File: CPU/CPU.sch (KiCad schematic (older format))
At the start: 12 parts, among them J101 Conn_02x10_Odd_Even, Q101 IRLML0040TR, Q102 IRLML0040TR, SW101 SW_SPDT

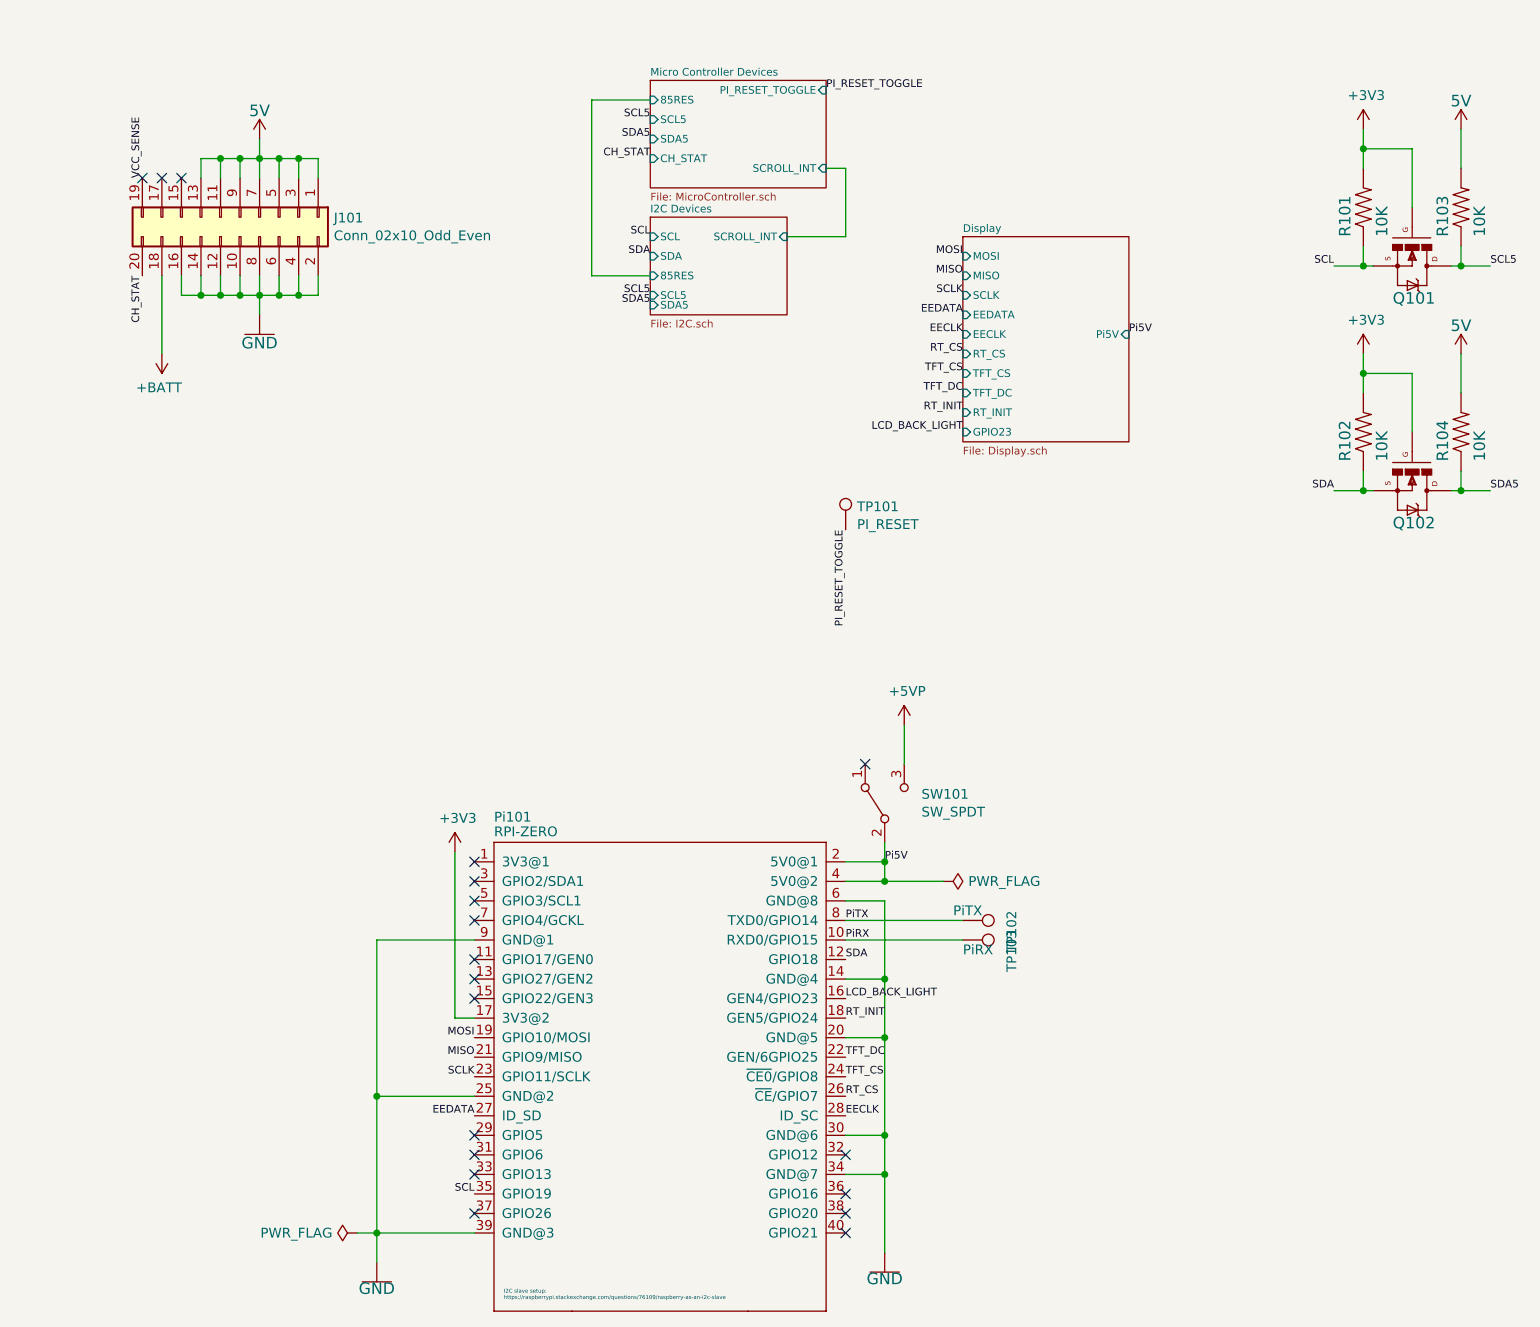
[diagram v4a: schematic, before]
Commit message: Move to separate branch to track CPU development separately.
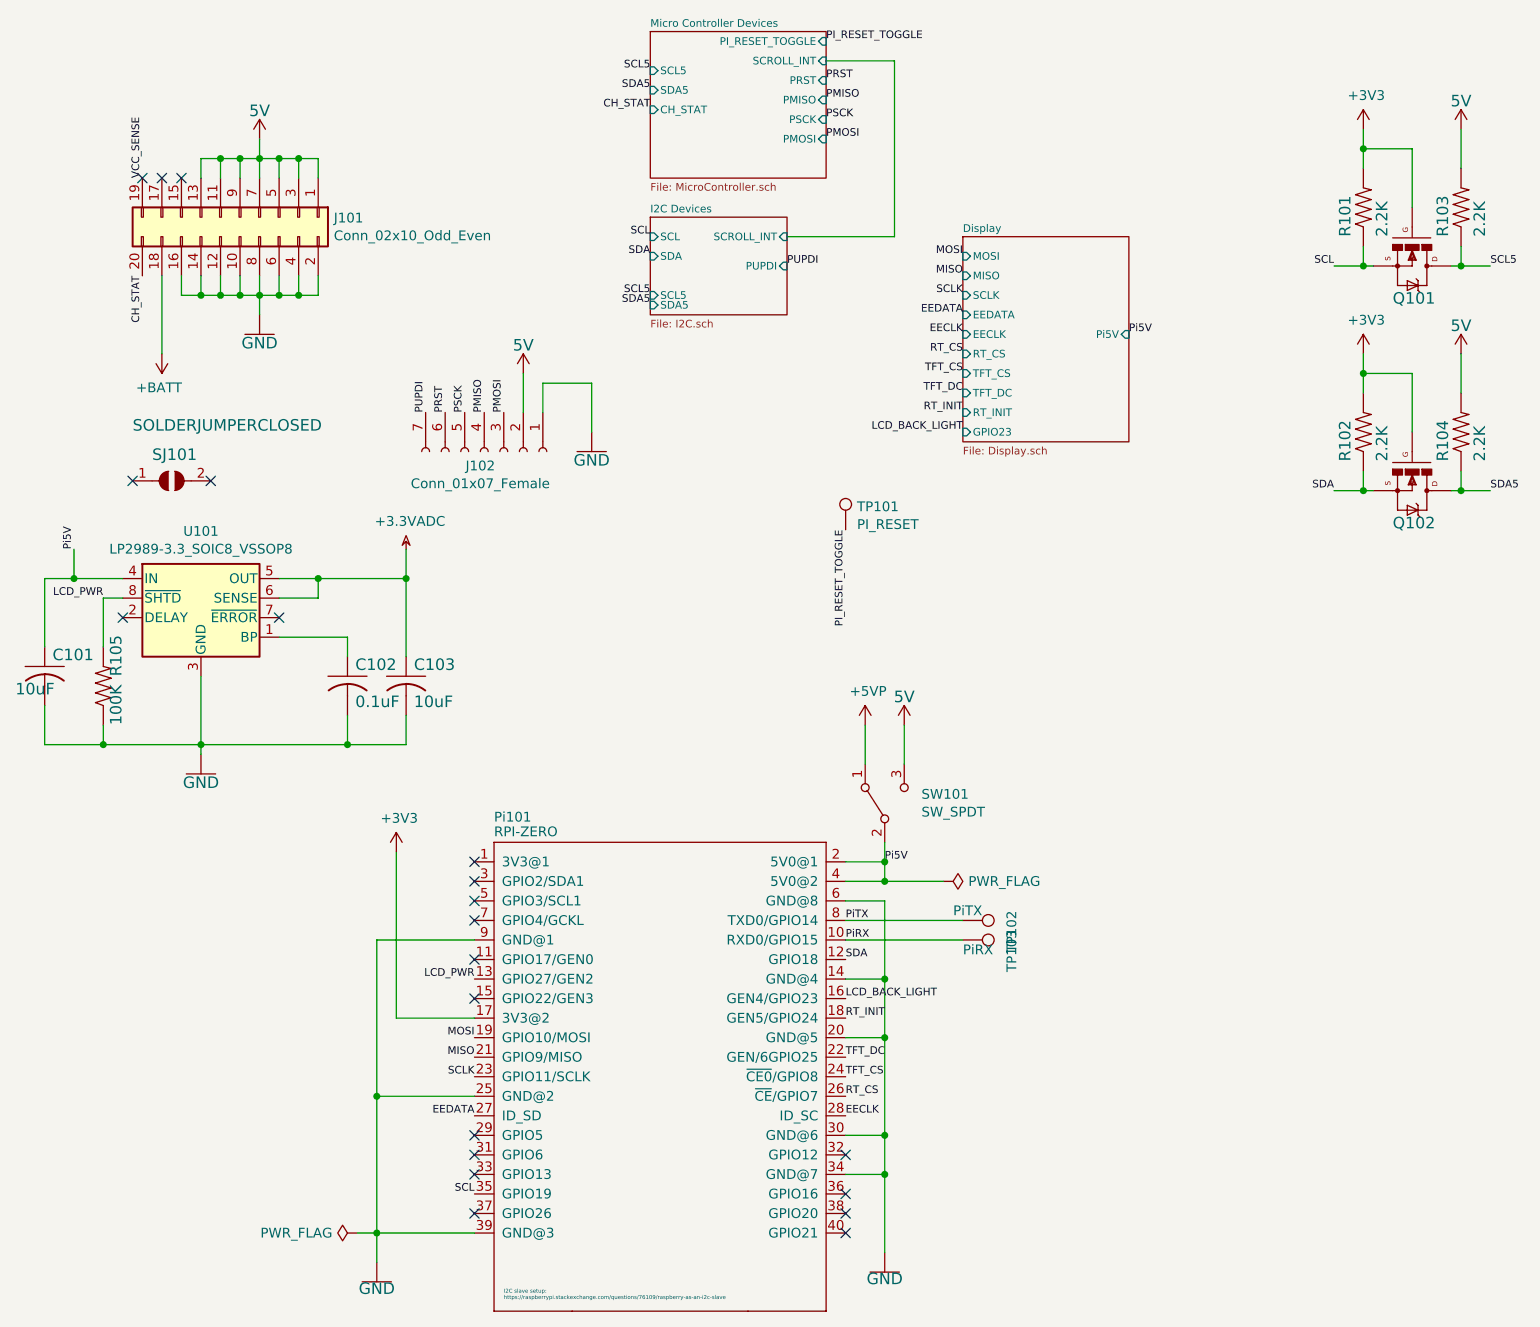
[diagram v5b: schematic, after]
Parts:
- added C101, C103: 10uF, Capacitor_SMD:C_0805_2012Metric_Pad1.15x1.40mm_HandSolder, symbol CPU-eagle-import:C-USC1210
- added C102: 0.1uF, Capacitor_SMD:C_0805_2012Metric_Pad1.15x1.40mm_HandSolder, symbol CPU-eagle-import:C-USC1210
- added J102: Conn_01x07_Female, MarcoK:SM07B-SHLS-TF, symbol Connector:Conn_01x07_Female
- added R105: 100K, Resistor_SMD:R_0805_2012Metric_Pad1.15x1.40mm_HandSolder, symbol CPU-eagle-import:R-US_R1206
- added SJ101: SOLDERJUMPERCLOSED, PiTFT:SOLDERJUMPER_CLOSEDWIRE, symbol PiTFT-eagle-import:SOLDERJUMPERCLOSED
- added U101: LP2989-3.3_SOIC8_VSSOP8, Package_SO:TSSOP-8_3x3mm_P0.65mm, symbol Regulator_Linear:LP2988-3.3_SOIC8_VSSOP8
- J101: DigiKey NRPN102MAMS-RC -> NRPN102MAMP-RC
- R101, R102, R103, R104: value 10K -> 2.2K
- SW101: Comment (none) -> MUST BE MAKE BEFORE BREAK!; DigiKey PCM12SMTR -> SS312SAH4-R
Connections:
- net +5VP: now also SW101.1 (A); no longer SW101.3 (C)
- net Pi5V: now also C101.1, U101.4 (IN)
- net LCD_PWR: now reaches Pi101.13 (GPIO27/GEN2)
- net LCD_PWR: now also R105.2, U101.8 (~SHTD)
- new net: C102.1, U101.1 (BP)
- new net: C101.2, C102.2, C103.2, R105.1, U101.3 (GND)
- new net +3.3VADC: C103.1, U101.5 (OUT), U101.6 (SENSE)
- new net PMISO: J102.4 (Pin_4)
- new net PMOSI: J102.3 (Pin_3)
- new net PRST: J102.6 (Pin_6)
- new net PSCK: J102.5 (Pin_5)
- new net PUPDI: J102.7 (Pin_7)
- no-connect marks 19 -> 21

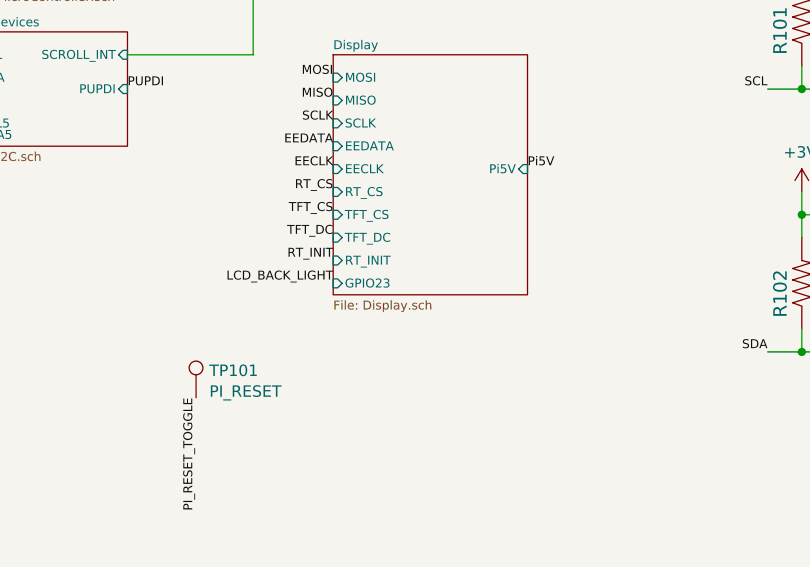
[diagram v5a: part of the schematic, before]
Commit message: Replacing the TFT. Before removing EEPROM and voltage monitor.
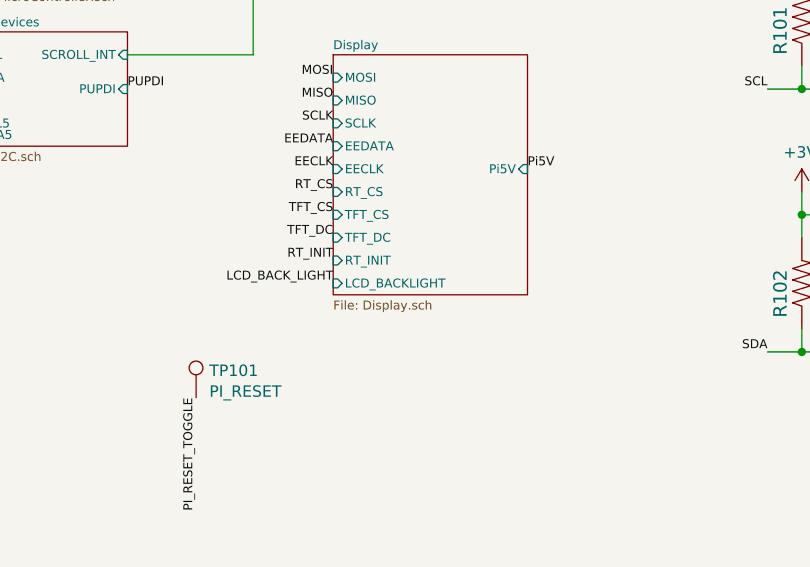
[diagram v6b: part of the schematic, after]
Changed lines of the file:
@@
 F9 "TFT_DC" I L 5550 2600 39
 F10 "RT_INIT" I L 5550 2700 39
-F11 "GPIO23" I L 5550 2800 39
+F11 "LCD_BACKLIGHT" I L 5550 2800 39
 F12 "Pi5V" I R 6400 2300 39
 $EndSheet

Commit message: BuyDisplay LCD.
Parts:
- removed C101, C103: 10uF, Capacitor_SMD:C_0805_2012Metric_Pad1.15x1.40mm_HandSolder, symbol CPU-eagle-import:C-USC1210
- removed C102: 0.1uF, Capacitor_SMD:C_0805_2012Metric_Pad1.15x1.40mm_HandSolder, symbol CPU-eagle-import:C-USC1210
- removed R105: 100K, Resistor_SMD:R_0805_2012Metric_Pad1.15x1.40mm_HandSolder, symbol CPU-eagle-import:R-US_R1206
- removed SJ101: SOLDERJUMPERCLOSED, PiTFT:SOLDERJUMPER_CLOSEDWIRE, symbol PiTFT-eagle-import:SOLDERJUMPERCLOSED
- removed U101: LP2989-3.3_SOIC8_VSSOP8, Package_SO:TSSOP-8_3x3mm_P0.65mm, symbol Regulator_Linear:LP2988-3.3_SOIC8_VSSOP8
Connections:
- net EECLK: no longer Pi101.28 (ID_SC)
- net EEDATA: no longer Pi101.27 (ID_SD)
- net LCD_BACK_LIGHT: now also Pi101.29 (GPIO5); no longer Pi101.16 (GEN4/GPIO23)
- net SCL: now also Pi101.5 (GPIO3/SCL1)
- net SDA: now also Pi101.3 (GPIO2/SDA1)
- net TFT_DC: now also Pi101.28 (ID_SC); no longer Pi101.22 (GEN/6GPIO25)
- new net TFT_RST: Pi101.27 (ID_SD)
- no-connect marks 21 -> 19
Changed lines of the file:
@@
 $EndDescr
-$Comp
-L CPU-eagle-import:RPI-ZERO Pi101
-U 1 1 87B7DF34
-P 3950 6200
-F 0 "Pi101" H 3150 7600 50  0000 L BNN
-F 1 "RPI-ZERO" H 3150 7525 50  0000 L BNN
-F 2 "CPU:RASPBERRYPI_Zero-No_Mounting_Holes_SMD_Flat" H 3950 6200 50  0001 C CNN
-F 3 "" H 3950 6200 50  0001 C CNN
-F 4 "609-2231-ND" H 3950 6200 50  0001 C CNN "DigiKey"
-F 5 "CR101-V3" H 3950 6200 50  0001 C CNN "Customer Reference"
-	1    3950 6200
-	1    0    0    -1
-$EndComp
 $Comp
 L Connector_Generic:Conn_02x10_Odd_Even J101
@@
 Text Label 3050 6100 2    39   ~ 0
 SCLK
-Text Label 3050 6300 2    39   ~ 0
-EEDATA
-Text Label 4950 6300 0    39   ~ 0
-EECLK
-Text Label 4950 6200 0    39   ~ 0
-RT_CS
 Text Label 4950 6100 0    39   ~ 0
 TFT_CS
-Text Label 4950 6000 0    39   ~ 0
-TFT_DC
 Text Label 4950 5800 0    39   ~ 0
 RT_INIT
@@
 Text Label 5150 5000 0    39   ~ 0
 Pi5V
-NoConn ~ 3050 6400
 NoConn ~ 3050 6500
 NoConn ~ 3050 6600
@@
 Text Notes 3200 7250 0    20   ~ 0
 I2C slave setup:\nhttps://raspberrypi.stackexchange.com/questions/76109/raspberry-as-an-i2c-slave
-NoConn ~ 3050 5100
-NoConn ~ 3050 5200
 $Comp
 L power:+5VP #PWR0108
@@
 F11 "LCD_BACKLIGHT" I L 5550 2800 39
 F12 "Pi5V" I R 6400 2300 39
+F13 "TFT_RST" I R 6400 2150 39
 $EndSheet
 Text Label 5550 2700 2    39   ~ 0
@@
 Text Label 5550 2800 2    39   ~ 0
 LCD_BACK_LIGHT
-Text Label 4950 5700 0    39   ~ 0
+Text Label 3050 6400 2    39   ~ 0
 LCD_BACK_LIGHT
 $Comp
@@
 Wire Wire Line
 	3300 2500 3300 2700
-$Comp
-L Regulator_Linear:LP2988-3.3_SOIC8_VSSOP8 U101
-U 1 1 5ED9EE3F
-P 1650 3650
-F 0 "U101" H 1650 3992 50  0000 C CNN
-F 1 "LP2989-3.3_SOIC8_VSSOP8" H 1650 3901 50  0000 C CNN
-F 2 "Package_SO:TSSOP-8_3x3mm_P0.65mm" H 1650 4075 50  0001 C CIN
-F 3 "http://www.ti.com/lit/ds/symlink/lp2987.pdf" H 1650 3650 50  0001 C CNN
-F 4 "LP2989IMM-3.3/NOPB" H 1650 3650 50  0001 C CNN "DigiKey"
-	1    1650 3650
-	1    0    0    -1
-$EndComp
-Wire Wire Line
-	1250 3550 1000 3550
-Wire Wire Line
-	1000 3550 1000 3400
-Wire Wire Line
-	2050 3550 2250 3550
-Wire Wire Line
-	2250 3550 2250 3650
-Wire Wire Line
-	2250 3650 2050 3650
-$Comp
-L CPU-eagle-import:GND #GND0104
-U 1 1 5EDA6100
-P 1650 4550
-F 0 "#GND0104" H 1650 4550 50  0001 C CNN
-F 1 "GND" H 1650 4540 59  0000 C TNN
-F 2 "" H 1650 4550 50  0001 C CNN
-F 3 "" H 1650 4550 50  0001 C CNN
-	1    1650 4550
-	1    0    0    -1
-$EndComp
-$Comp
-L CPU-eagle-import:C-USC1210 C103
-U 1 1 5EDAAE71
-P 2700 4050
-AR Path="/5EDAAE71" Ref="C103"  Part="1"
-AR Path="/5E9D5ED5/5EDAAE71" Ref="C?"  Part="1"
-F 0 "C103" H 2740 4075 59  0000 L BNN
-F 1 "10uF" H 2740 3885 59  0000 L BNN
-F 2 "Capacitor_SMD:C_0805_2012Metric_Pad1.15x1.40mm_HandSolder" H 2700 4050 50  0001 C CNN
-F 3 "" H 2700 4050 50  0001 C CNN
-F 4 " C15850" H 2700 4050 50  0001 C CNN "LCSC Part Number"
-F 5 "EMK212ABJ106MD-T" H 2700 4050 50  0001 C CNN "DigiKey"
-F 6 "CR101-V3" H 2700 4050 50  0001 C CNN "Customer Reference"
-	1    2700 4050
-	1    0    0    -1
-$EndComp
-Connection ~ 2250 3550
-$Comp
-L CPU-eagle-import:C-USC1210 C102
-U 1 1 5EDB4B5E
-P 2400 4050
-AR Path="/5EDB4B5E" Ref="C102"  Part="1"
-AR Path="/5E9D5ED5/5EDB4B5E" Ref="C?"  Part="1"
-F 0 "C102" H 2440 4075 59  0000 L BNN
-F 1 "0.1uF" H 2440 3885 59  0000 L BNN
-F 2 "Capacitor_SMD:C_0805_2012Metric_Pad1.15x1.40mm_HandSolder" H 2400 4050 50  0001 C CNN
-F 3 "" H 2400 4050 50  0001 C CNN
-F 4 " C1848 " H 2400 4050 50  0001 C CNN "LCSC Part Number"
-F 5 "C0805C104K3RACTU" H 2400 4050 50  0001 C CNN "DigiKey"
-F 6 "CR101-V3" H 2400 4050 50  0001 C CNN "Customer Reference"
-	1    2400 4050
-	1    0    0    -1
-$EndComp
-Wire Wire Line
-	2700 3550 2700 3950
-Wire Wire Line
-	2250 3550 2700 3550
-Wire Wire Line
-	2050 3850 2400 3850
-Wire Wire Line
-	2400 3850 2400 3950
-Wire Wire Line
-	1650 4050 1650 4400
-Wire Wire Line
-	2700 4250 2700 4400
-Wire Wire Line
-	2700 4400 2400 4400
-Connection ~ 1650 4400
-Wire Wire Line
-	1650 4400 1650 4450
-Wire Wire Line
-	2400 4250 2400 4400
-Connection ~ 2400 4400
-Wire Wire Line
-	2400 4400 1650 4400
-$Comp
-L CPU-eagle-import:C-USC1210 C101
-U 1 1 5EDC66D5
-P 850 4000
-AR Path="/5EDC66D5" Ref="C101"  Part="1"
-AR Path="/5E9D5ED5/5EDC66D5" Ref="C?"  Part="1"
-F 0 "C101" H 890 4025 59  0000 L BNN
-F 1 "10uF" H 700 3850 59  0000 L BNN
-F 2 "Capacitor_SMD:C_0805_2012Metric_Pad1.15x1.40mm_HandSolder" H 850 4000 50  0001 C CNN
-F 3 "" H 850 4000 50  0001 C CNN
-F 4 " C15850" H 850 4000 50  0001 C CNN "LCSC Part Number"
-F 5 "EMK212ABJ106MD-T" H 850 4000 50  0001 C CNN "DigiKey"
-F 6 "CR101-V3" H 850 4000 50  0001 C CNN "Customer Reference"
-	1    850  4000
-	1    0    0    -1
-$EndComp
-Wire Wire Line
-	1000 3550 850  3550
-Wire Wire Line
-	850  3550 850  3900
-Connection ~ 1000 3550
-Wire Wire Line
-	1650 4400 1150 4400
-Wire Wire Line
-	850  4400 850  4200
-$Comp
-L PiTFT-eagle-import:SOLDERJUMPERCLOSED SJ?
-U 1 1 5EDD1B31
-P 1500 3050
-AR Path="/5EC4945A/5EDD1B31" Ref="SJ?"  Part="1"
-AR Path="/5EDD1B31" Ref="SJ101"  Part="1"
-F 0 "SJ101" H 1400 3150 59  0000 L BNN
-F 1 "SOLDERJUMPERCLOSED" H 1300 3300 59  0000 L BNN
-F 2 "PiTFT:SOLDERJUMPER_CLOSEDWIRE" H 1500 3050 50  0001 C CNN
-F 3 "" H 1500 3050 50  0001 C CNN
-F 4 "CR101-V3" H 1500 3050 50  0001 C CNN "Customer Reference"
-	1    1500 3050
-	1    0    0    -1
-$EndComp
 Text Label 3050 5600 2    39   ~ 0
 LCD_PWR
@@
 Wire Wire Line
 	2650 5800 3050 5800
-Text Label 1150 3650 2    39   ~ 0
-LCD_PWR
-NoConn ~ 2050 3750
-NoConn ~ 1250 3750
-$Comp
-L CPU-eagle-import:R-US_R1206 R?
-U 1 1 5EDE06CA
-P 1150 4100
-AR Path="/5E916134/5EDE06CA" Ref="R?"  Part="1"
-AR Path="/5EDE06CA" Ref="R105"  Part="1"
-F 0 "R105" H 1200 4000 59  0000 L BNN
-F 1 "100K" H 950 4000 59  0000 L BNN
-F 2 "Resistor_SMD:R_0805_2012Metric_Pad1.15x1.40mm_HandSolder" H 1150 4100 50  0001 C CNN
-F 3 "" H 1150 4100 50  0001 C CNN
-F 4 " C17414" H 1150 4100 50  0001 C CNN "LCSC Part Number"
-F 5 "RC0805FR-0710KL" H 1150 4100 50  0001 C CNN "DigiKey"
-F 6 "CR101-V3" H 1150 4100 50  0001 C CNN "Customer Reference"
-	1    1150 4100
-	0    -1   -1   0
-$EndComp
-Wire Wire Line
-	1150 4300 1150 4400
-Connection ~ 1150 4400
-Wire Wire Line
-	1150 4400 850  4400
-Wire Wire Line
-	1250 3650 1150 3650
-Wire Wire Line
-	1150 3650 1150 3900
-NoConn ~ 1700 3050
-NoConn ~ 1300 3050
-Text Label 1000 3400 1    39   ~ 0
-Pi5V
-$Comp
-L power:+3.3VADC #PWR0103
-U 1 1 5EDFA204
-P 2700 3400
-F 0 "#PWR0103" H 2850 3350 50  0001 C CNN
-F 1 "+3.3VADC" H 2720 3543 50  0000 C CNN
-F 2 "" H 2700 3400 50  0001 C CNN
-F 3 "" H 2700 3400 50  0001 C CNN
-	1    2700 3400
-	1    0    0    -1
-$EndComp
-Wire Wire Line
-	2700 3550 2700 3400
-Connection ~ 2700 3550
 $Comp
 L CPU-eagle-import:5V #SUPPLY?
@@
 Wire Wire Line
 	5050 4500 5050 4300
+$Comp
+L CPU-eagle-import:RPI-ZERO Pi101
+U 1 1 87B7DF34
+P 3950 6200
+F 0 "Pi101" H 3150 7600 50  0000 L BNN
+F 1 "RPI-ZERO" H 3150 7525 50  0000 L BNN
+F 2 "CPU:RASPBERRYPI_Zero-No_Mounting_Holes_SMD_Flat" H 3950 6200 50  0001 C CNN
+F 3 "" H 3950 6200 50  0001 C CNN
+F 4 "609-2231-ND" H 3950 6200 50  0001 C CNN "DigiKey"
+F 5 "CR101-V3" H 3950 6200 50  0001 C CNN "Customer Reference"
+	1    3950 6200
+	1    0    0    -1
+$EndComp
+Text Label 4950 6200 0    39   ~ 0
+RT_CS
+Text Label 4950 6300 0    39   ~ 0
+TFT_DC
+NoConn ~ 4950 5700
+NoConn ~ 4950 6000
+NoConn ~ 3050 6000
+NoConn ~ 4950 6200
+NoConn ~ 4950 5800
+Text Label 6400 2150 0    39   ~ 0
+TFT_RST
+Text Label 3050 6300 2    39   ~ 0
+TFT_RST
+Text Label 3050 5200 2    39   ~ 0
+SCL
+Text Label 3050 5100 2    39   ~ 0
+SDA
 $EndSCHEMATC
